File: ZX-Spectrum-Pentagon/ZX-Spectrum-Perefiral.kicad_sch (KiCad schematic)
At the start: 4 parts, among them U1 74HC00

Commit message: add zxm_extrime_extension add 74XX283 to 74IEC start ZX-Spectrum-Perefiral project
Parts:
- removed C1: C, Capacitor_SMD:C_0805_2012Metric_Pad1.18x1.45mm_HandSolder, symbol Device:C
- removed R1, R2: R, Resistor_SMD:R_0805_2012Metric_Pad1.20x1.40mm_HandSolder, symbol Device:R
- removed U1: 74HC00, symbol 74IEC:74HC00
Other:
- added sheet Connectors (ZX-Spectrum-Perefiral/Connectors.kicad_sch)
- added sheet FDDC (ZX-Spectrum-Perefiral/FDDC.kicad_sch)
- added sheet Power (ZX-Spectrum-Perefiral/Popwer.kicad_sch)

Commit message: update schematic FDC
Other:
- sheet FDDC ports: added A0, A1, A10, A11, A12, A13, A14, A15, A2, A3, A4, A5, A6, A7, A8, A9, D0, D1, D2, D3, D4, D5, D6, D7, ~{IORQ}, ~{M1}, ~{MREQ}, ~{WAIT}; removed none

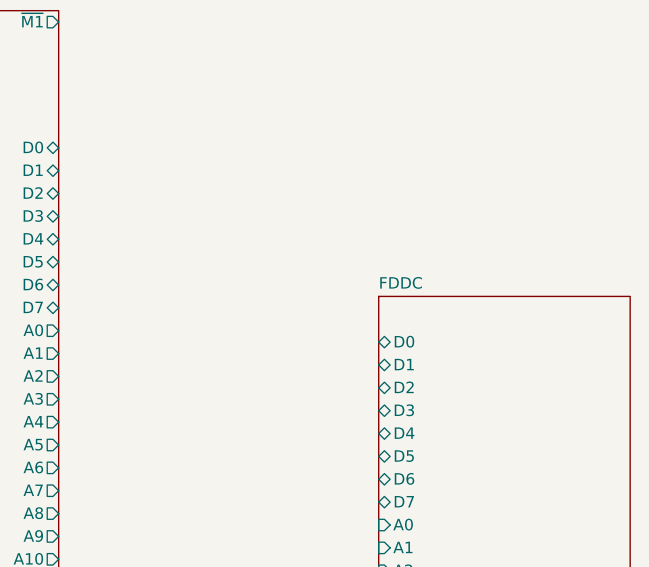
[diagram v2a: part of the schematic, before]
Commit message: rename FDDC fdc
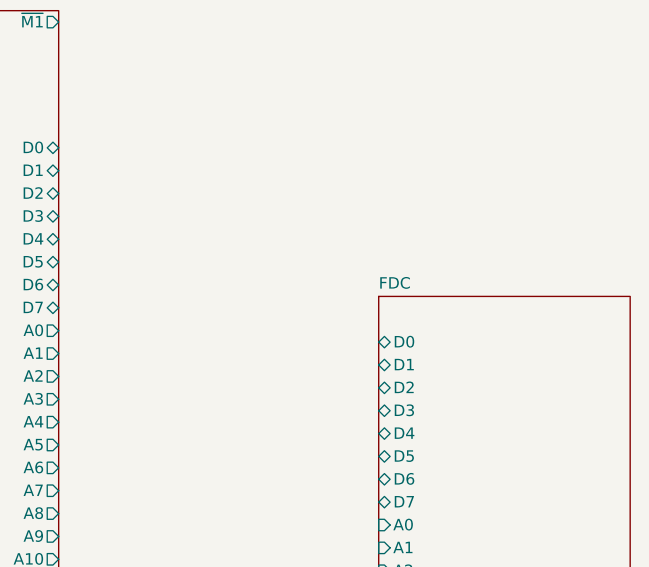
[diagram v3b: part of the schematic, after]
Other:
- sheet FDDC renamed FDC
- sheet FDC: file ZX-Spectrum-Perefiral/FDDC.kicad_sch -> ZX-Spectrum-Perefiral/FDC.kicad_sch
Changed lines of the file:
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@@
 			(color 0 0 0 0.0000)
 		)
-		(property "Sheetname" "FDDC"
+		(property "Sheetname" "FDC"
 			(at 99.06 70.4084 0)
 			(effects
@@
 			)
 		)
-		(property "Sheetfile" "ZX-Spectrum-Perefiral/FDDC.kicad_sch"
+		(property "Sheetfile" "ZX-Spectrum-Perefiral/FDC.kicad_sch"
 			(at 99.06 146.6346 0)
 			(effects

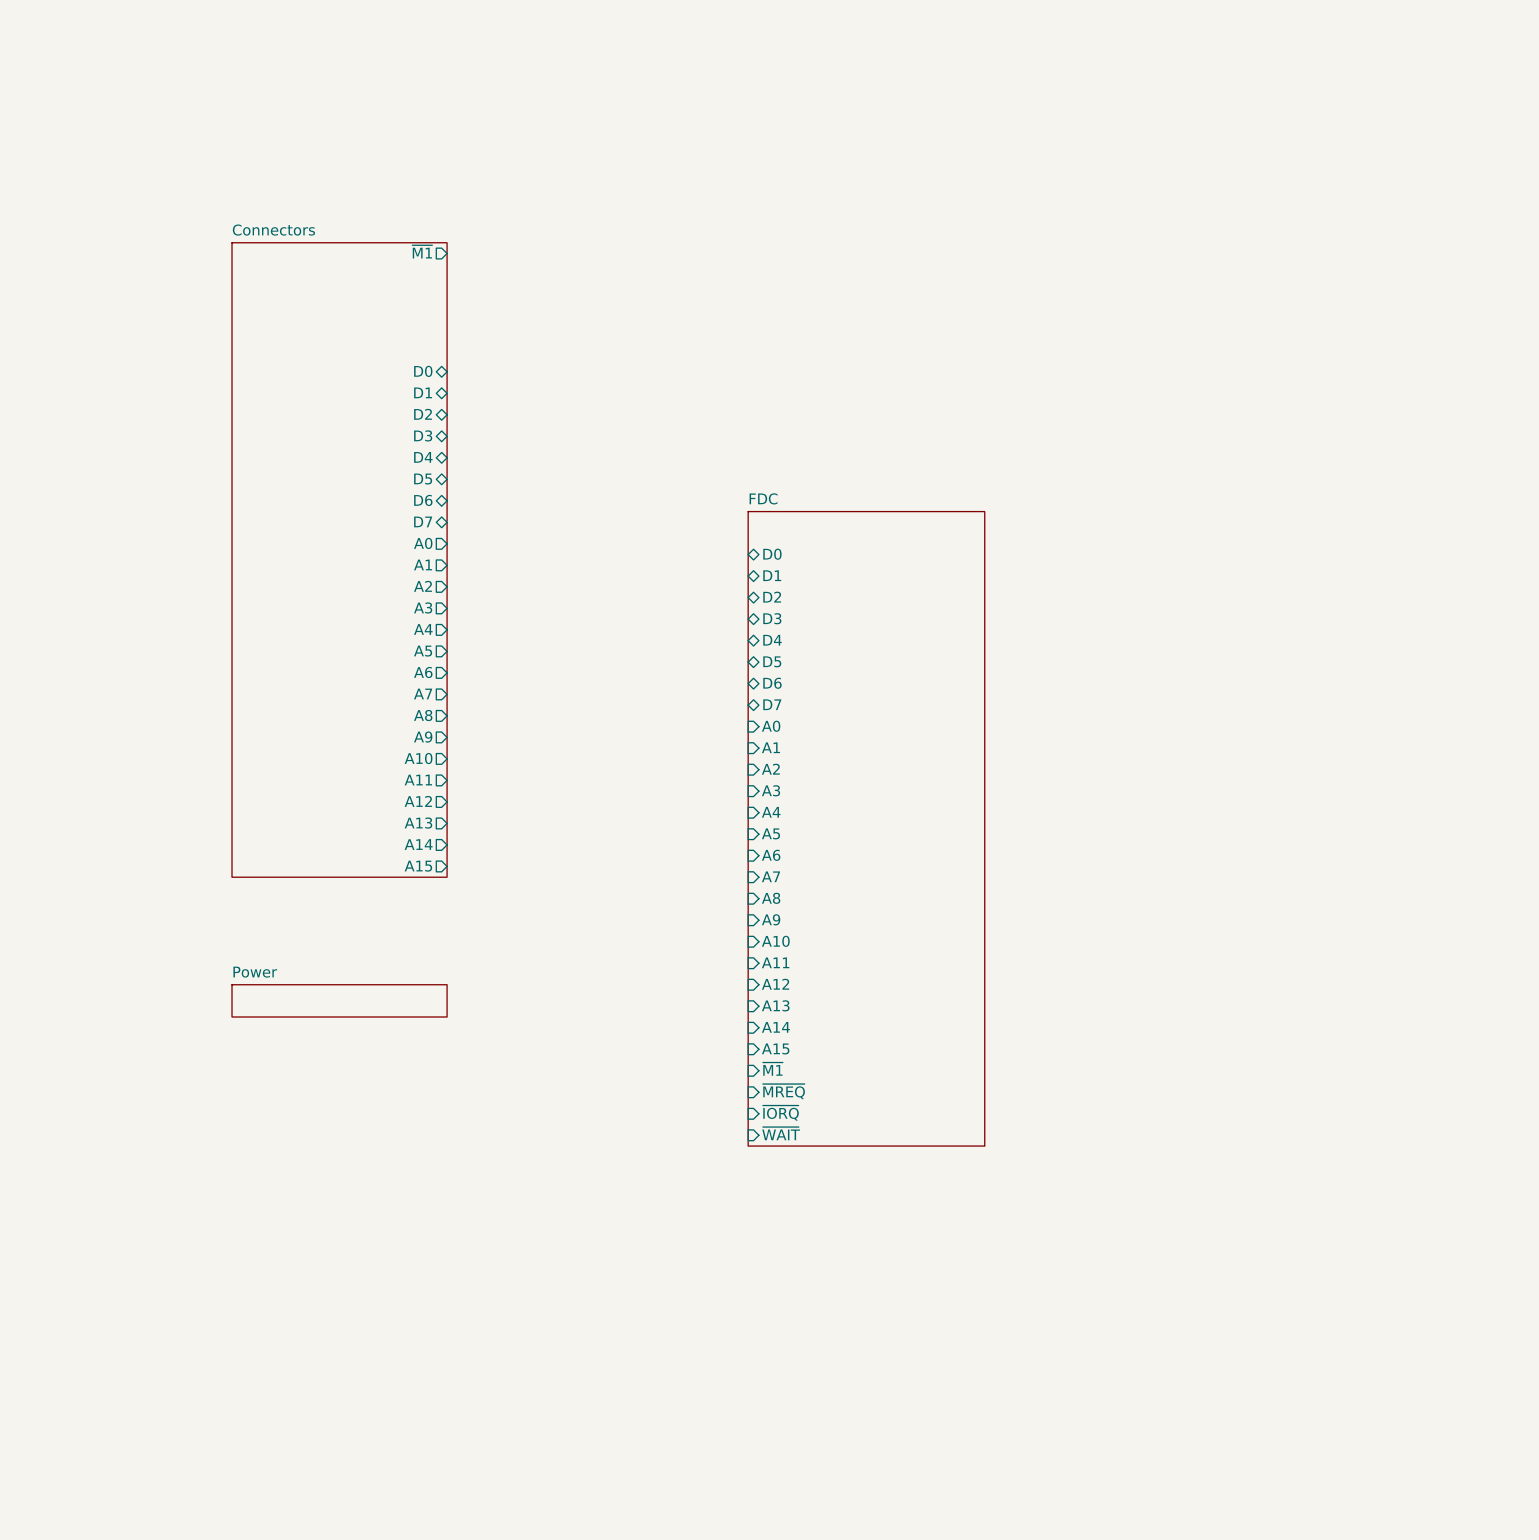
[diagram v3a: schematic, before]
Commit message: add keywords for some symbol in library 74IEC update some symbol in zx_custom_symbol improve FDC, Connectors, ZX-Spectrum-Perefiral schematic
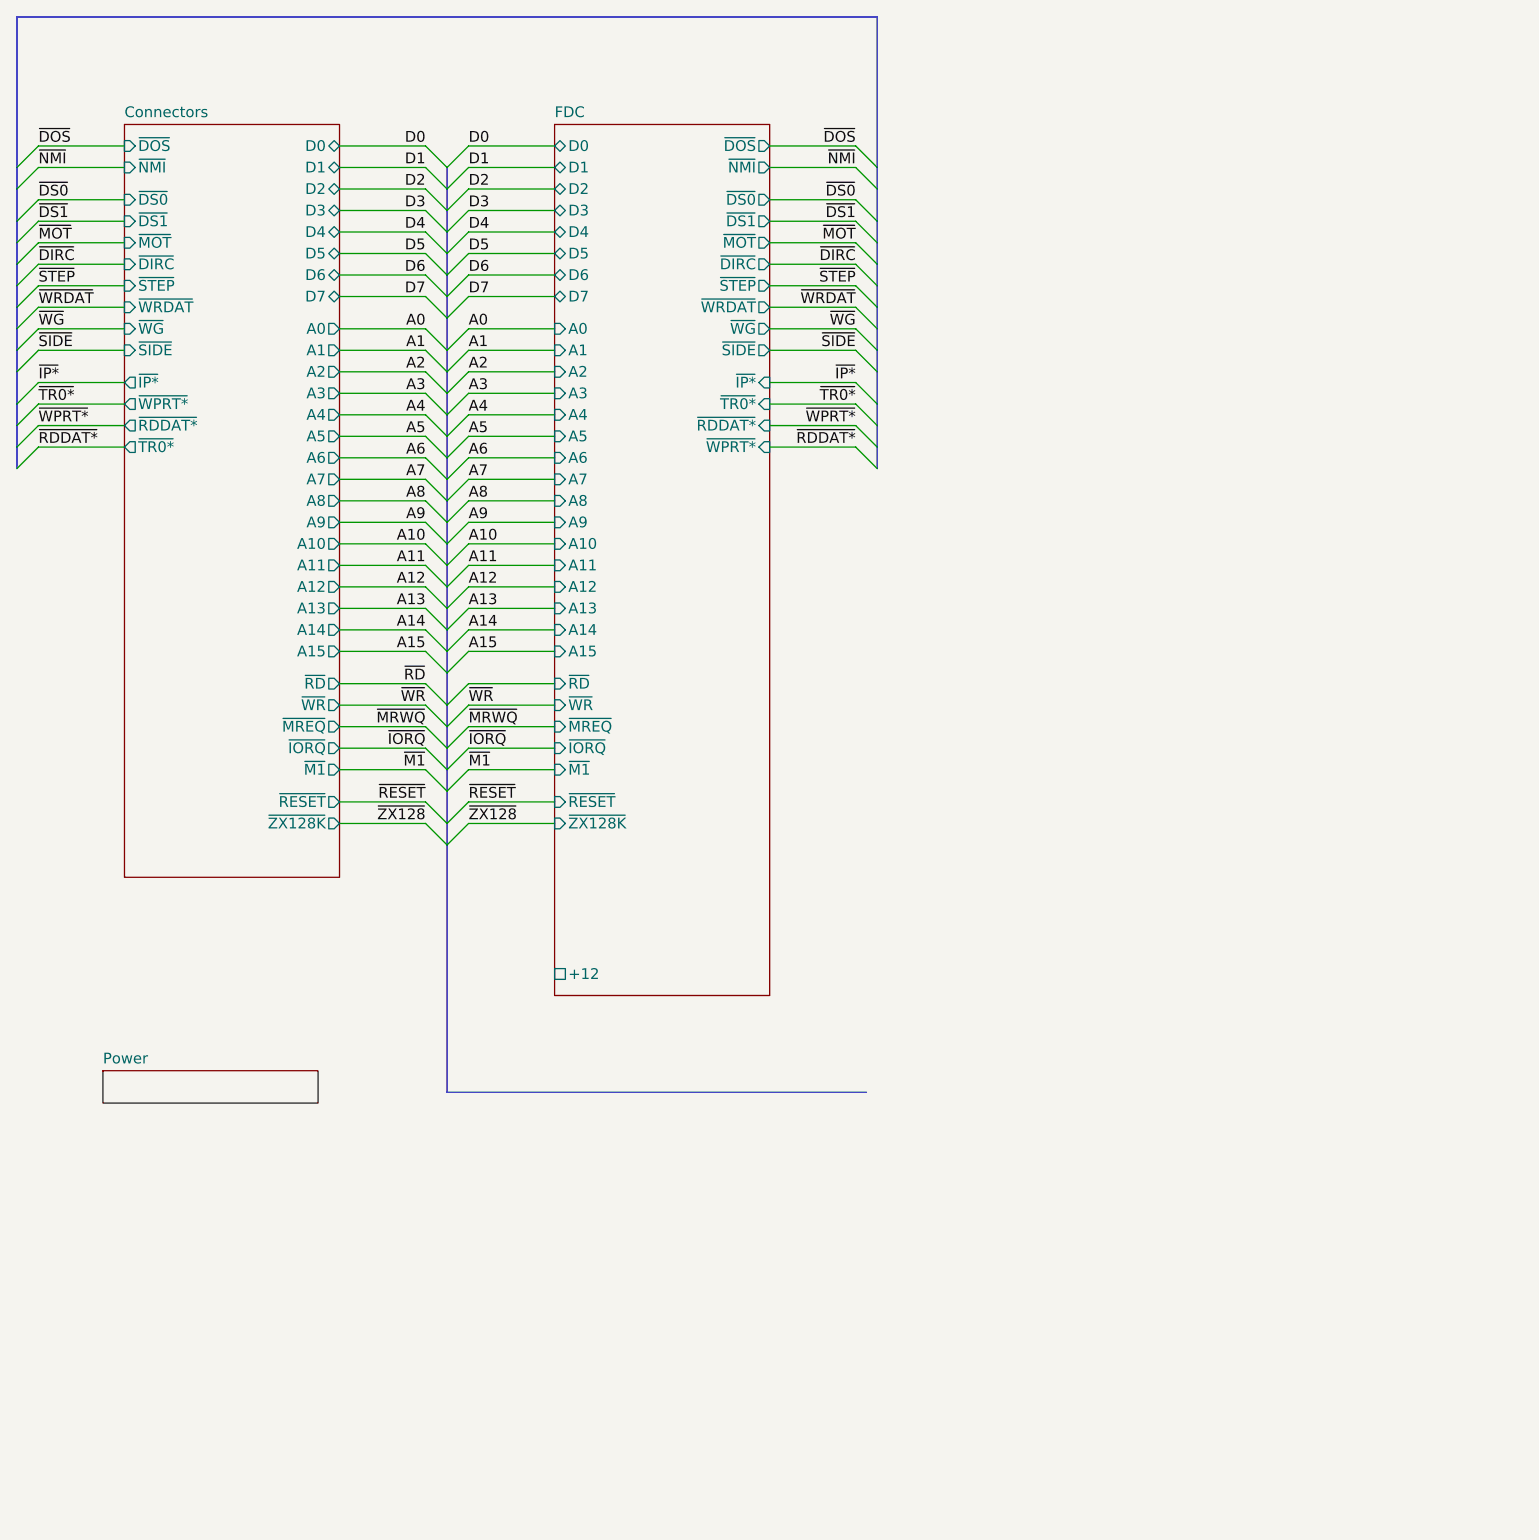
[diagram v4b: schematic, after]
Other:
- sheet Connectors ports: added ~{DIRC}, ~{DOS}, ~{DS0}, ~{DS1}, ~{IORQ}, ~{IP*}, ~{MOT}, ~{MREQ}, ~{NMI}, ~{RDDAT*}, ~{RD}, ~{RESET}, ~{SIDE}, ~{STEP}, ~{TR0*}, ~{WG}, ~{WPRT*}, ~{WRDAT}, ~{WR}, ~{ZX128K}; removed none
- sheet FDC ports: added +12, ~{DIRC}, ~{DOS}, ~{DS0}, ~{DS1}, ~{IP*}, ~{MOT}, ~{NMI}, ~{RDDAT*}, ~{RD}, ~{RESET}, ~{SIDE}, ~{STEP}, ~{TR0*}, ~{WG}, ~{WPRT*}, ~{WRDAT}, ~{WR}, ~{ZX128K}; removed ~{WAIT}
- title: (none) -> ZX-Pentagon-Pereferal

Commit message: update ZX-Spectrum-Perefiral
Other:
- added sheet IDE (ZX-Spectrum-Perefiral/IDE.kicad_sch)
- sheet Connectors ports: added HA0, HA1, HA2, HD0, HD1, HD10, HD11, HD12, HD13, HD14, HD15, HD2, HD3, HD4, HD5, HD6, HD7, HD8, HD9, ~{ACT}, ~{HCS0}, ~{HCS1}, ~{HIOR}, ~{HIOW}, ~{HRESET}; removed none

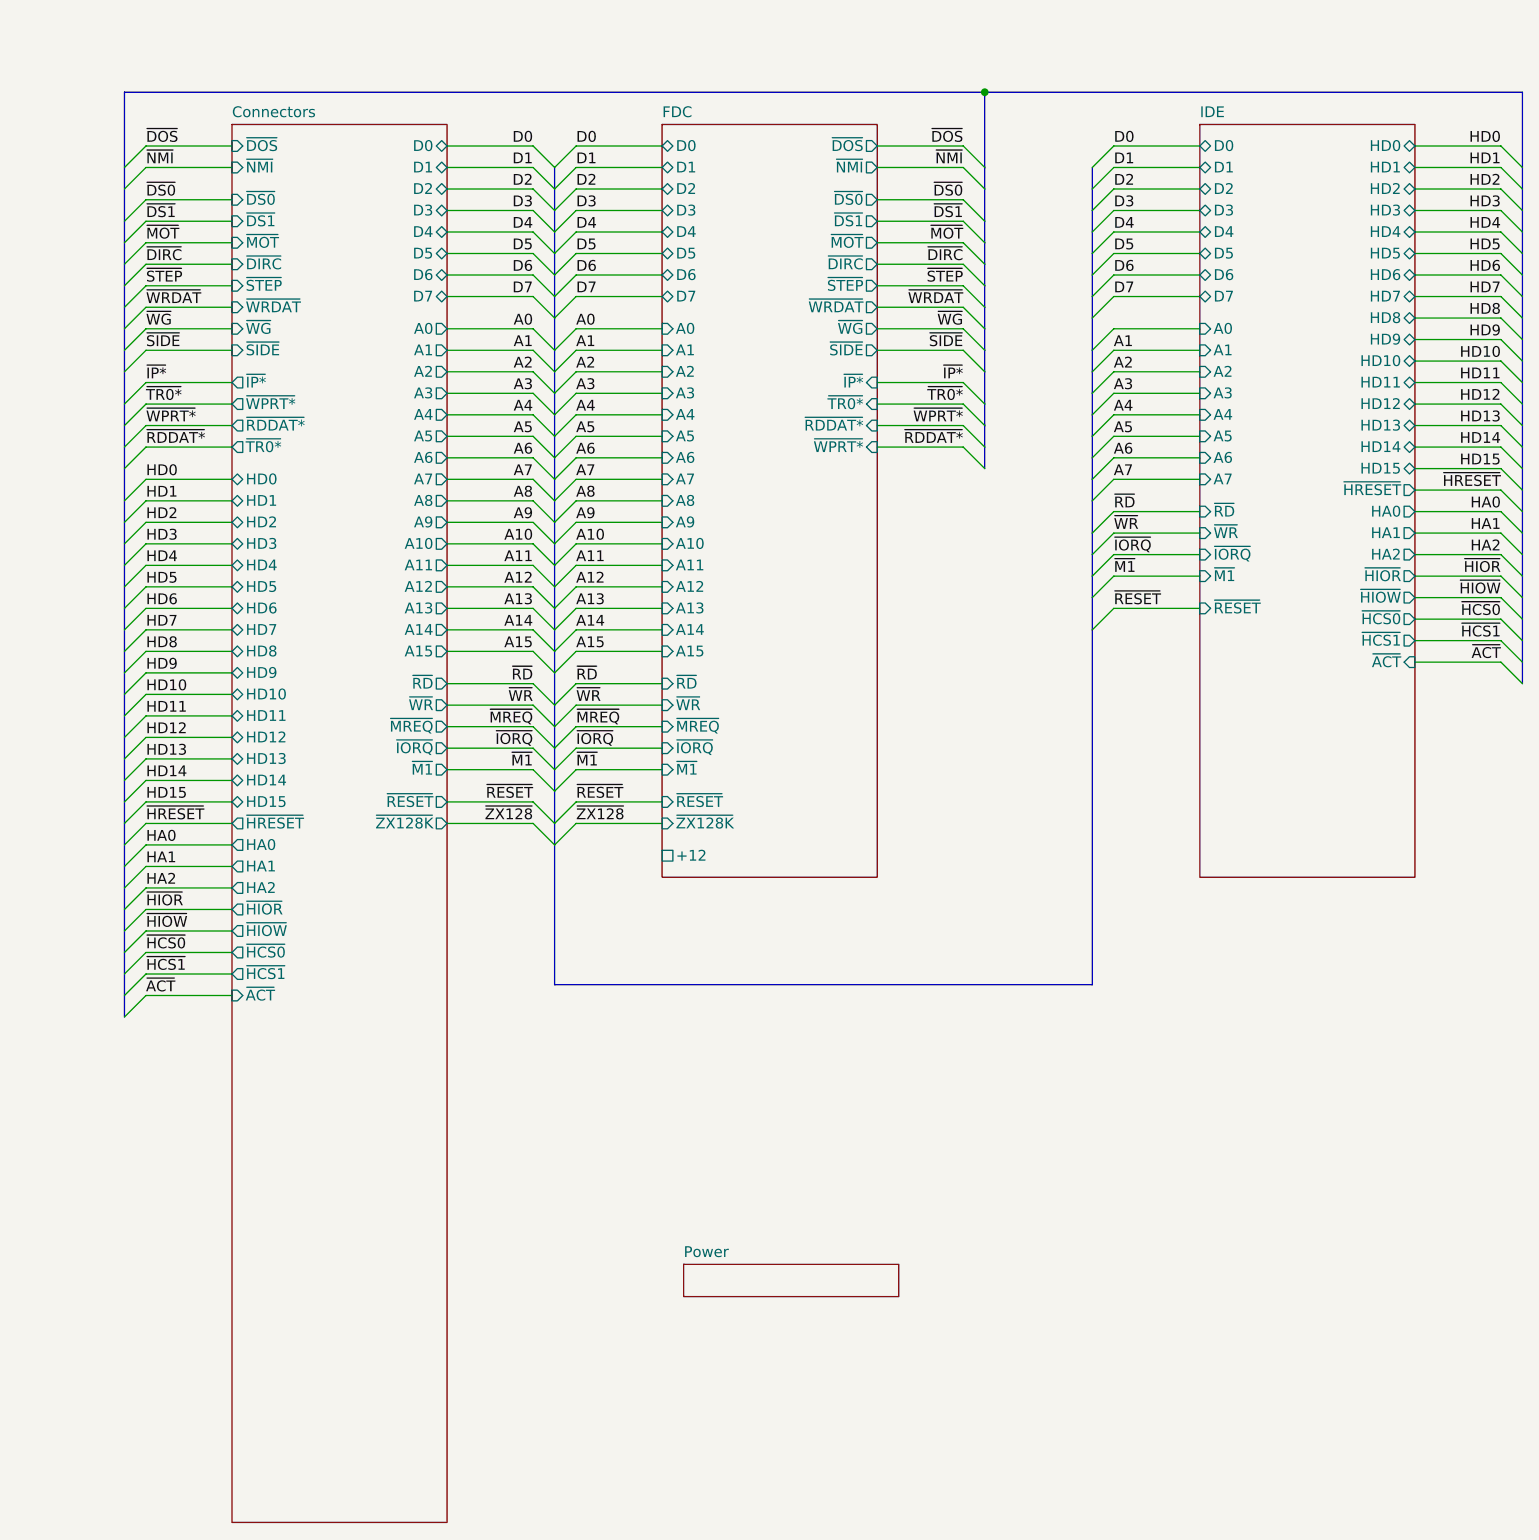
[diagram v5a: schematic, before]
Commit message: fix 74ICE, FDControlers, edge_lib library update all schematic and board fix ERC ZX-Spectrum-Perefiral
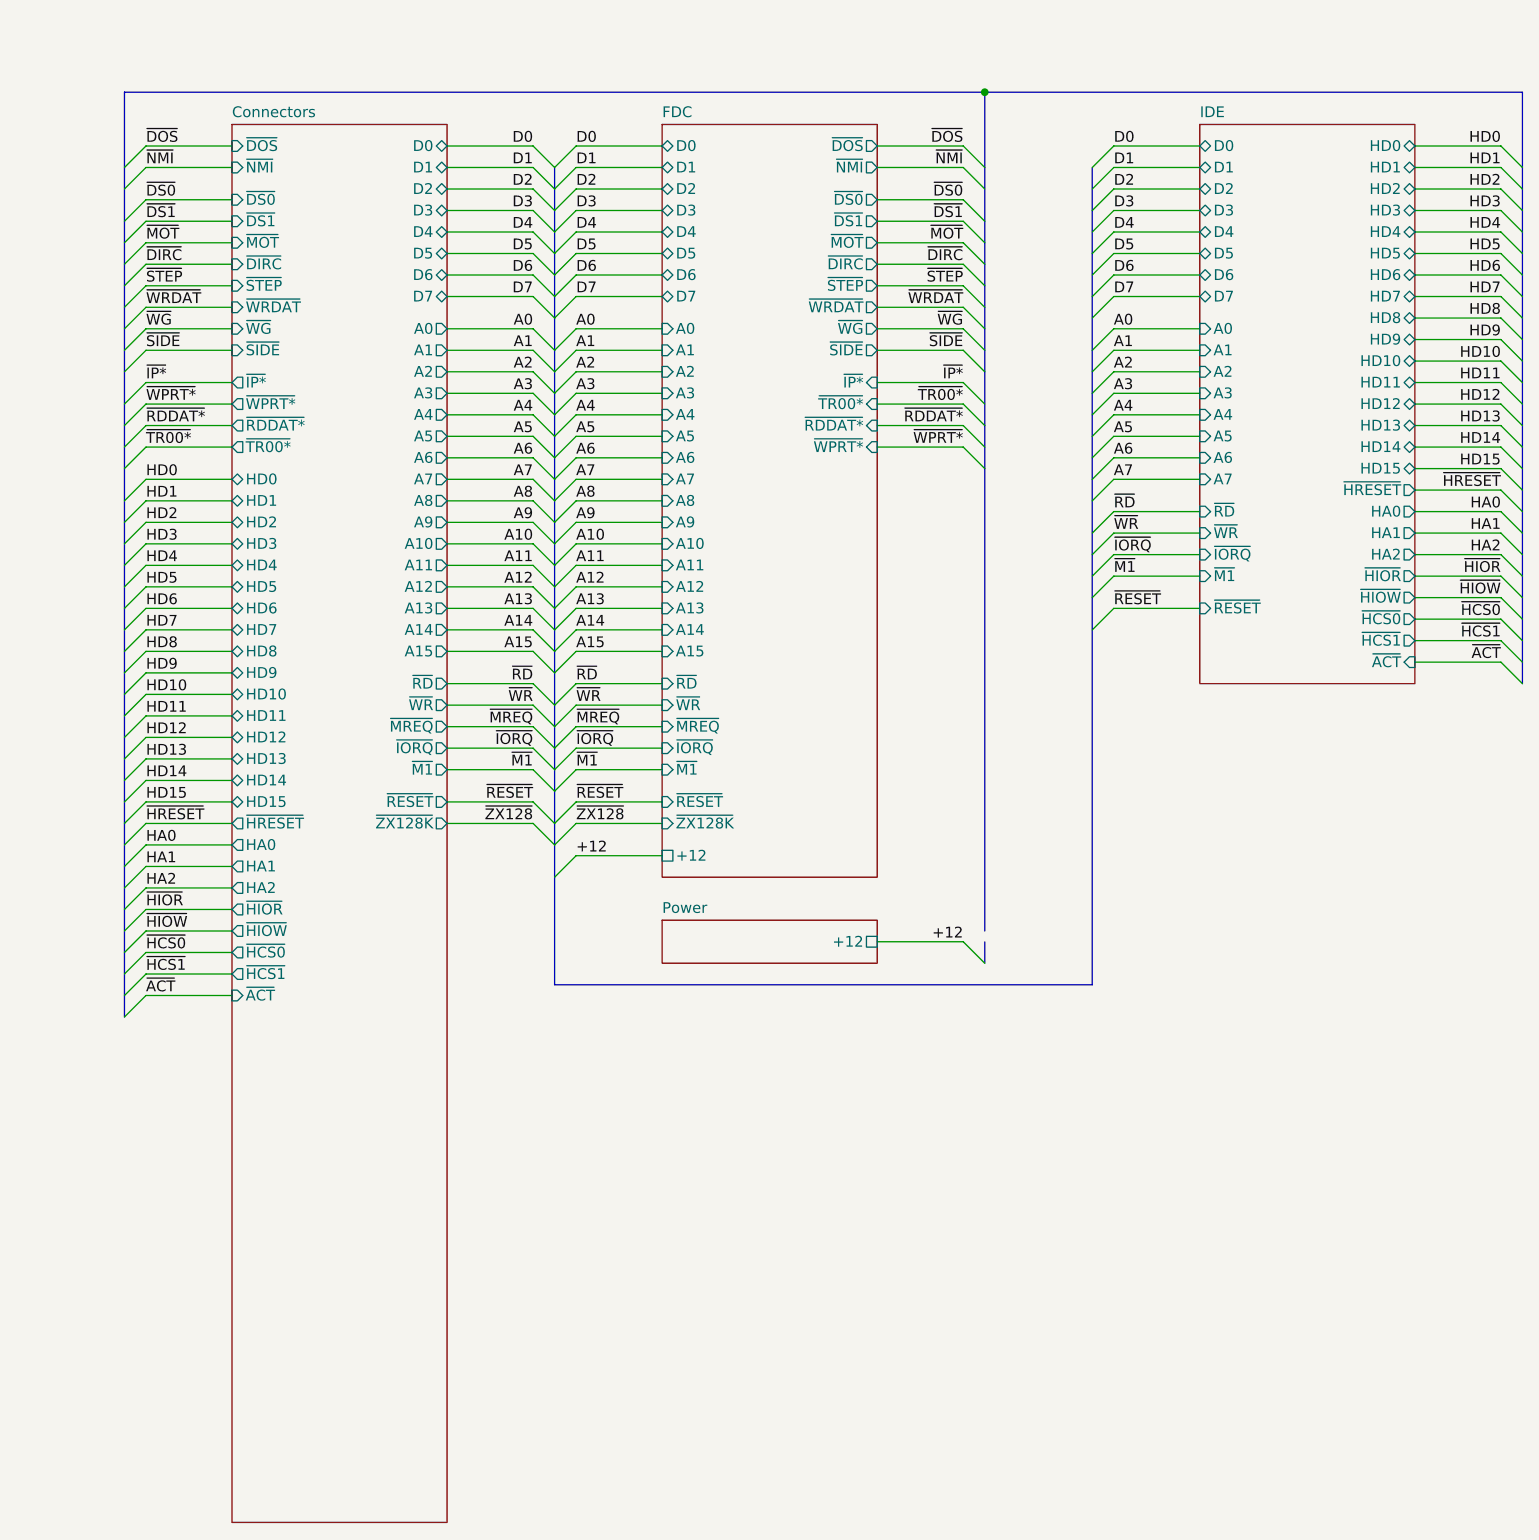
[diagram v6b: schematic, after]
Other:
- sheet Connectors ports: added ~{TR00*}; removed ~{TR0*}
- sheet FDC ports: added ~{TR00*}; removed ~{TR0*}
- sheet Power ports: added +12; removed none
